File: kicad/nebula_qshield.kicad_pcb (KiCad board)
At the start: 4 copper layers, 150 x 120 mm, 164 parts, among them J1 J1, J10 J10, J11 J11, J12 J12, J13 J13, J14 J14, J15 J15, J16 J16, J17 J17, J18 J18, J19 J19, J2 J2, J20 J20, J21 Arduino UNO Q Shield, J3 J3, J4 J4, J5 J5, J6 J6, J7 J7, J8 J8, J9 J9, K1 HF46F-12-HS1, K2 HF46F-12-HS1, Q1 IRLZ44NPBF, Q2 IRLZ44NPBF, Q3 2N7002, Q4 2N7002, Q5 IRLZ44NPBF, SW1 RESET, T1 Transformer_SP_2S, T2 Transformer_SP_2S, T3 Transformer_SP_2S, U1 TPS54302DDCR, U10 MCP6002, U11 MCP6002, U12 SN6501, U13 AMC1301, U14 HX711, U15 MAX485ESA, U16 PC817X2NIP, U17 IR2104SPBF, U18 PC817X1NIP, U19 PC817X1NIP, U2 AMS1117-3.3, U20 MCP6002, U21 ISO1541, U22 SC16IS740, U23 SN74LVC1G04, U3 TPS3823-33DBVR, U4 MCP6002, U5 SN6501, U6 AMC1301, U7 MCP6002, U8 SN6501, U9 AMC1301, Y1 1.8432MHz

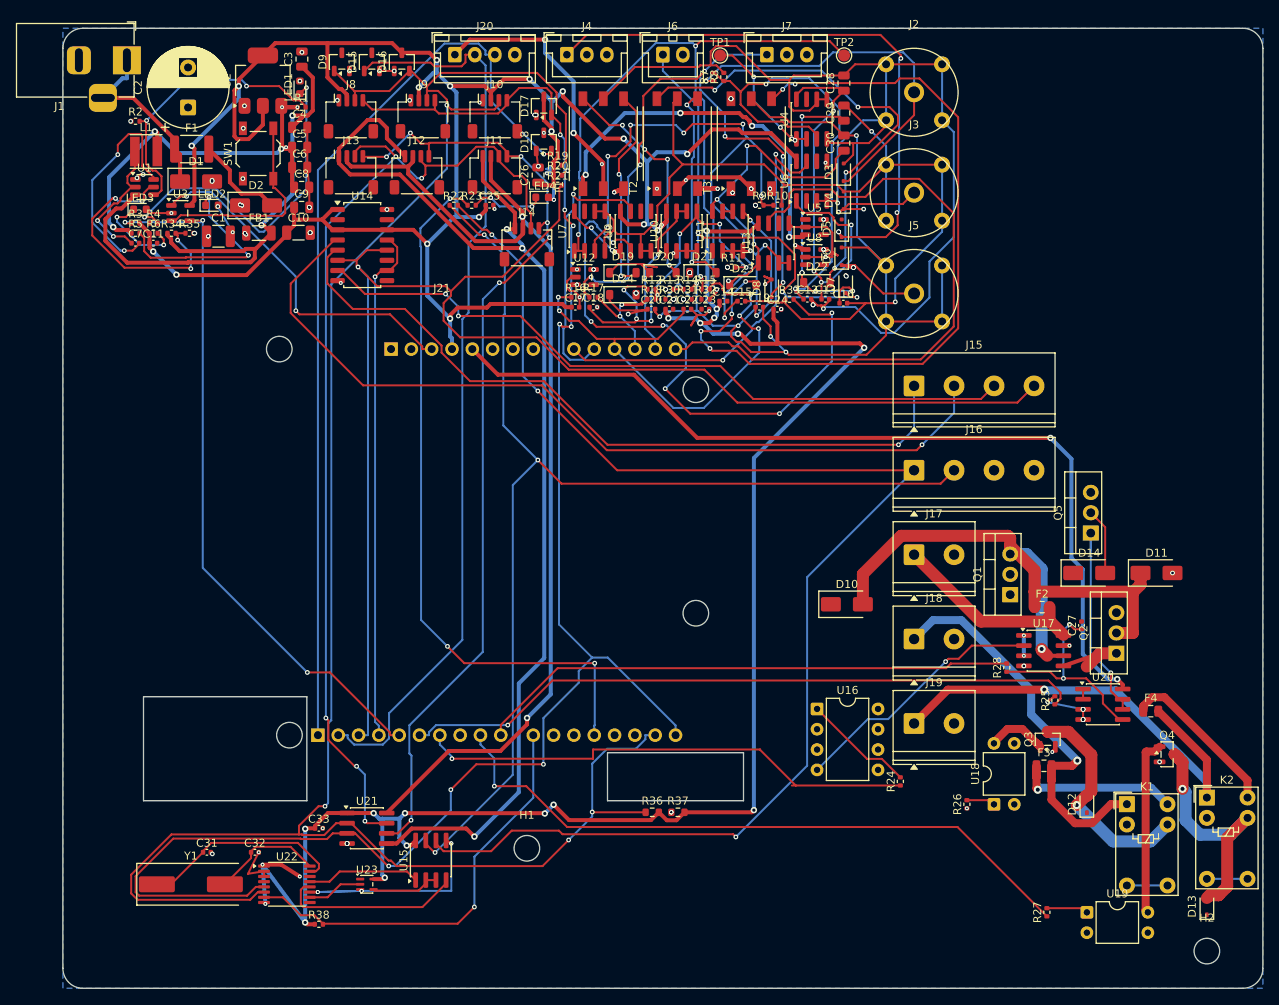
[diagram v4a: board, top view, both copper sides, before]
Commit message: Fase 6: apply Spark short-pair routing, close U22 GND, add close_pairs_v7.py; DRC 0, 44 unconnected
Co-Authored-By: Devin AI <158243242+devin-ai-integration[bot]@users.noreply.github.com>
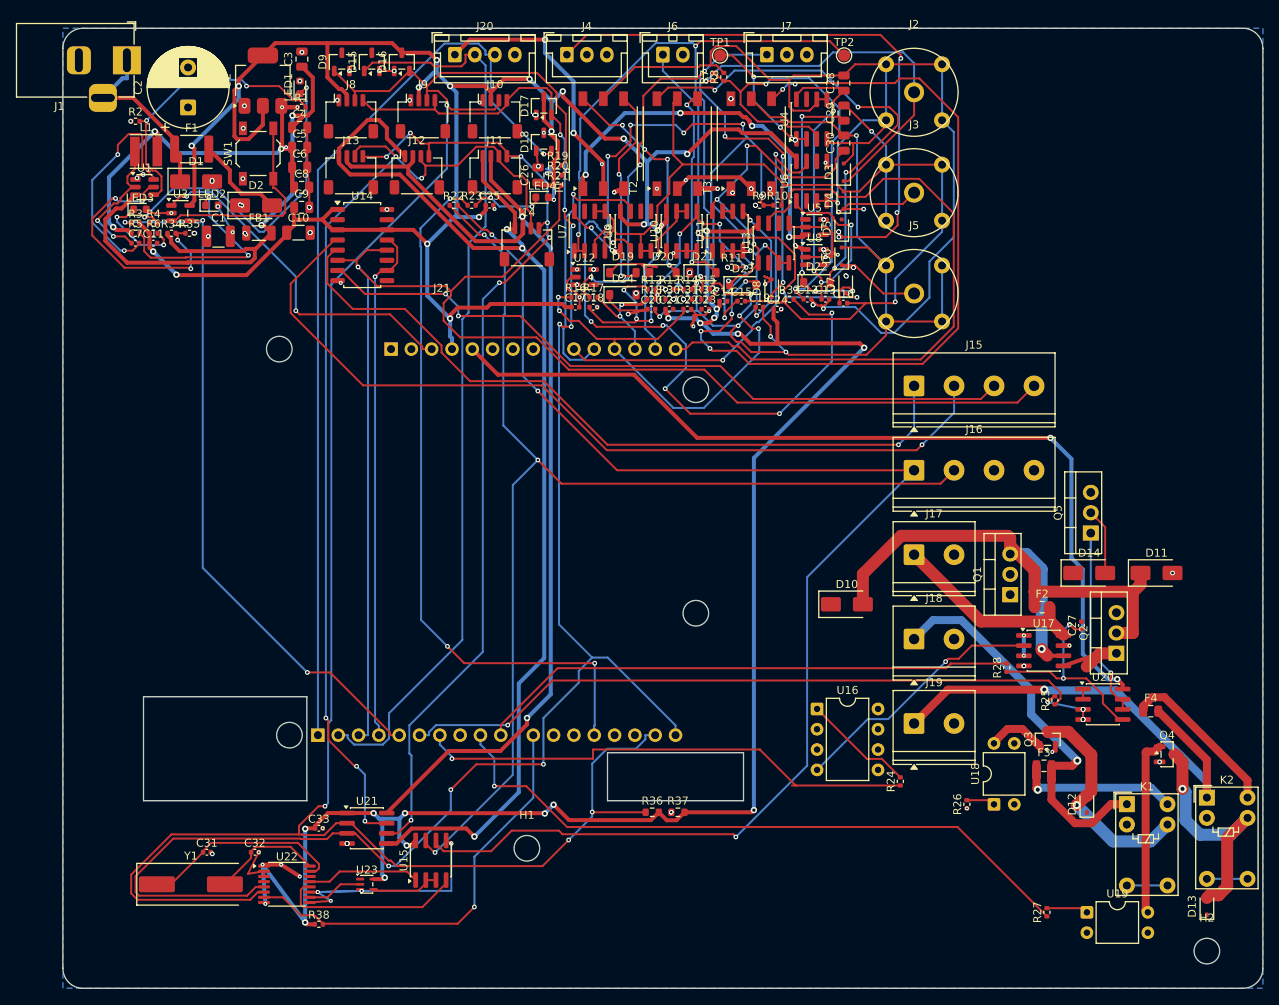
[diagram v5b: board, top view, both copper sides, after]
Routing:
- net GND: track 140.9 -> 148.1 mm, vias 81 -> 84
- net /Analog Acquisition/VDD_ISO_DO: track 50.7 -> 53.7 mm
- net /Analog Acquisition/PH_ATT: track 5.17 -> 7.75 mm
- net /Analog Acquisition/SN_D2_ORP: track 7.50 -> 10.0 mm
- net /Analog Acquisition/ORP_SIG: track 13.6 -> 16.1 mm
- net /HUM_ADC: track 17.1 -> 19.2 mm
- net /Analog Acquisition/VDD_ISO_PH: track 62.8 -> 64.8 mm
- net /Analog Acquisition/DO_SIG: track 16.5 -> 18.0 mm
- net /Analog Acquisition/SN_D2_PH: track 5.00 -> 6.25 mm
- net /Analog Acquisition/VDD_ISO_ORP: track 47.7 -> 48.4 mm
- net /Actuator Drivers/MOTOR_HO: track 0.75 -> 1.50 mm
- net /Analog Acquisition/GND_ISO_PH: track 150.5 -> 151.2 mm
- net /Analog Acquisition/CO2_SIG: track 74.4 -> 74.8 mm, vias 6 -> 7
- net /Analog Acquisition/PH_BUF: track 17.6 -> 17.8 mm, vias 6 -> 7
- net /5V_RAIL: vias 21 -> 22
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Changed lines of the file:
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@@
 		(net "/HUM_ADC")
 	)
+	(segment
+		(start 61.8669 32.5372)
+		(end 63.96845 32.5372)
+		(width 0.25)
+		(layer "F.Cu")
+		(net "/HUM_ADC")
+	)
 	(via
 		(at 61.642 33.9906)
@@
 	)
 	(segment
+		(start 22.8625 107.275)
+		(end 25.5 107.075)
+		(width 0.25)
+		(layer "F.Cu")
+		(net "GND")
+	)
+	(segment
 		(start 66.09 31.87)
 		(end 66.34 31.87)
@@
 	)
 	(segment
+		(start 70.813675 33.8472)
+		(end 70.813675 35.273785)
+		(width 0.25)
+		(layer "F.Cu")
+		(net "GND")
+	)
+	(segment
 		(start 88.185 26.0062)
 		(end 88.834519 26.3812)
@@
 	)
 	(segment
+		(start 71.2772 33.8472)
+		(end 70.813675 33.8472)
+		(width 0.25)
+		(layer "F.Cu")
+		(net "GND")
+	)
+	(segment
 		(start 1.6871 16.2754)
 		(end 2.0369 16.2754)
@@
 	)
 	(segment
+		(start 88.185 26.0062)
+		(end 88.870159 26.311252)
+		(width 0.25)
+		(layer "F.Cu")
+		(net "GND")
+	)
+	(segment
 		(start 71.2772 33.8472)
 		(end 70.54 33.11)
@@
 	)
 	(via
+		(at 70.813675 35.273785)
+		(size 0.5)
+		(drill 0.2)
+		(layers "F.Cu" "B.Cu")
+		(net "GND")
+	)
+	(via
 		(at 51.4 15.24)
 		(size 0.5)
@@
 	)
 	(via
+		(at 25.5 107.075)
+		(size 0.5)
+		(drill 0.2)
+		(layers "F.Cu" "B.Cu")
+		(net "GND")
+	)
+	(via
 		(at 51.17 8.8375)
 		(size 0.6)
@@
 	)
 	(via
+		(at 88.870159 26.311252)
+		(size 0.5)
+		(drill 0.2)
+		(layers "F.Cu" "B.Cu")
+		(net "GND")
+	)
+	(via
 		(at 23.8625 105.975)
 		(size 0.5)
@@
 	)
 	(segment
+		(start 25.5 107.075)
+		(end 23.8625 105.975)
+		(width 0.25)
+		(layer "B.Cu")
+		(net "GND")
+	)
+	(segment
 		(start 52.12 9.4774)
 		(end 53.0798 10.4372)
@@
 	)
 	(via
+		(at 19.286612 102.548222)
+		(size 0.5)
+		(drill 0.2)
+		(layers "F.Cu" "B.Cu")
+		(net "/3V3_RAIL")
+	)
+	(via
 		(at 37.5491 24.9462)
 		(size 0.8)
@@
 	(segment
 		(start 61.695 25.825)
+		(end 60.961389 25.980934)
+		(width 0.25)
+		(layer "F.Cu")
+		(net "/Analog Acquisition/VDD_ISO_ORP")
+	)
+	(segment
+		(start 61.695 25.825)
 		(end 61.6183 25.7483)
 		(width 0.25)
@@
 	)
 	(segment
+		(start 85.54 31.86)
+		(end 85.771763 32.573292)
+		(width 0.25)
+		(layer "F.Cu")
+		(net "/Analog Acquisition/GND_ISO_PH")
+	)
+	(segment
 		(start 86.7776 32.6536)
 		(end 87.2216 32.6536)
@@
 	(segment
 		(start 89.6 20.6)
+		(end 92.1 20.6)
+		(width 0.25)
+		(layer "F.Cu")
+		(net "/Analog Acquisition/ORP_SIG")
+	)
+	(segment
+		(start 89.6 20.6)
 		(end 90.2332 19.9668)
 		(width 0.25)
@@
 		(net "/Analog Acquisition/PH_BUF")
 	)
+	(segment
+		(start 83.695 11.825)
+		(end 83.588934 11.931066)
+		(width 0.25)
+		(layer "F.Cu")
+		(net "/Analog Acquisition/PH_BUF")
+	)
 	(via
 		(at 78.3584 4.0749)
@@
 		(net "/Analog Acquisition/PH_BUF")
 	)
+	(via
+		(at 83.588934 11.931066)
+		(size 0.6)
+		(drill 0.3)
+		(layers "F.Cu" "B.Cu")
+		(net "/Analog Acquisition/PH_BUF")
+	)
 	(segment
 		(start 78.3584 4.0749)
@@
 	)
 	(segment
+		(start 64.2719 27.4719)
+		(end 66.247277 27.784769)
+		(width 0.25)
+		(layer "F.Cu")
+		(net "/Analog Acquisition/VDD_ISO_PH")
+	)
+	(segment
 		(start 88.3217 7.1083)
 		(end 88.3217 8.3387)
@@
 	)
 	(via
+		(at 83.623679 25.263729)
+		(size 0.5)
+		(drill 0.2)
+		(layers "F.Cu" "B.Cu")
+		(net "/5V_RAIL")
+	)
+	(via
 		(at 115.452 49.2027)
 		(size 0.8)
@@
 	)
 	(segment
+		(start 65.08 33.11)
+		(end 62.658542 33.731725)
+		(width 0.25)
+		(layer "F.Cu")
+		(net "/Analog Acquisition/VDD_ISO_DO")
+	)
+	(segment
 		(start 76.4811 28.9189)
 		(end 75.35 30.05)
@@
 	)
 	(segment
+		(start 75.35 30.05)
+		(end 75.195492 29.574472)
+		(width 0.25)
+		(layer "F.Cu")
+		(net "/Analog Acquisition/VDD_ISO_DO")
+	)
+	(segment
 		(start 60.35 31.3)
 		(end 60.35 32.0867)
@@
 		(net "/Actuator Drivers/MOTOR_HO")
 	)
+	(segment
+		(start 117.0714 75.1659)
+		(end 117.8214 75.1659)
+		(width 0.5)
+		(layer "F.Cu")
+		(net "/Actuator Drivers/MOTOR_HO")
+	)
 	(via
 		(at 110.4135 68.7984)
@@
 	)
 	(segment
+		(start 89.35 24.1)
+		(end 89 24.1)
+		(width 0.25)
+		(layer "F.Cu")
+		(net "/Analog Acquisition/CO2_SIG")
+	)
+	(segment
 		(start 96.7459 1.3772)
 		(end 94.195 -1.1737)
@@
 	)
 	(via
+		(at 89 24.1)
+		(size 0.6)
+		(drill 0.3)
+		(layers "F.Cu" "B.Cu")
+		(net "/Analog Acquisition/CO2_SIG")
+	)
+	(via
 		(at 75.07 27.87)
 		(size 0.6)
@@
 	)
 	(segment
+		(start 68.955 29.87)
+		(end 70.59 31.87)
+		(width 0.25)
+		(layer "B.Cu")
+		(net "/Analog Acquisition/PH_ATT")
+	)
+	(segment
 		(start 67.32 31.87)
 		(end 68.955 29.87)
@@
 	)
 	(segment
+		(start 89.35 27.6)
+		(end 90.817221 27.911868)
+		(width 0.25)
+		(layer "F.Cu")
+		(net "/Analog Acquisition/DO_SIG")
+	)
+	(segment
 		(start 90.996 27.6)
 		(end 94.546 31.15)
@@
 		(net "/Analog Acquisition/SN_D2_ORP")
 	)
+	(segment
+		(start 71.34 18.05)
+		(end 73.84 18.05)
+		(width 0.5)
+		(layer "F.Cu")
+		(net "/Analog Acquisition/SN_D2_ORP")
+	)
 	(via
 		(at 73.84 18.05)
@@
 		(width 0.5)
 		(layer "F.Cu")
+		(net "/Analog Acquisition/SN_D2_PH")
+	)
+	(segment
+		(start 62.09 18.05)
+		(end 60.927779 18.510156)
+		(width 0.5)
+		(layer "F.Cu")
